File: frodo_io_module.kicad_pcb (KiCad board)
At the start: 4 copper layers, 60 x 60 mm, 162 parts, among them J1 Conn_02x04_Top_Bottom, J10 JST-GH 4Pin, J11 JST-GH 4Pin, J14 Conn_02x03_Odd_Even, J16 USB_C_Receptacle_USB2.0, J17 TC2050, J2 Conn_02x10_Odd_Even, J3 Conn_02x04_Top_Bottom, J4 Conn_02x03_Odd_Even, J6 JST-GH 4Pin, J7 JST-GH 4Pin, J8 JST-GH 4Pin, J9 JST-GH 4Pin, Q1 AOSP21321, Q2 AOSP21321, Q3 NMOS, Q4 NMOS, Q5 AOSP21321, Q6 AOSP21321, Q7 NMOS, Q8 NMOS, SW1 KMR721NGLFS, SW2 KMR721NGLFS, SW3 KMR721NGLFS, U1 L7805, U10 MCP2562-E-SN, U11 TPD4E1U06, U12 INA181A1, U2 L7805, U3 STM32F105RCTx, U5 AZ1117-3.3, U6 W25Q128JVP, U7 MCP2562-E-SN, U8 TPD4E1U06, U9 INA181A1, Y1 8MHz 12pF

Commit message: small routing improvements
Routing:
- net +3.3V: track 368.6 -> 370.0 mm
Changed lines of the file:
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@@
 	)
 	(segment
-		(start 145.734 104.156)
-		(end 145.734 107.932496)
-		(width 0.5)
-		(layer "F.Cu")
-		(net 2)
-	)
-	(segment
 		(start 110.78 117.05)
 		(end 110.29 117.54)
@@
 	)
 	(segment
+		(start 145.734 107.932496)
+		(end 145.734 104.156)
+		(width 0.5)
+		(layer "F.Cu")
+		(net 2)
+	)
+	(segment
 		(start 119.216182 124.334)
 		(end 122.484 124.334)
@@
 	)
 	(segment
-		(start 145.74 104.15)
-		(end 145.734 104.156)
-		(width 0.5)
-		(layer "F.Cu")
-		(net 2)
-	)
-	(segment
 		(start 111.02 117.29)
 		(end 110.78 117.05)
@@
 	)
 	(segment
+		(start 145.734 104.156)
+		(end 145.74 104.15)
+		(width 0.5)
+		(layer "F.Cu")
+		(net 2)
+	)
+	(segment
 		(start 121.230002 104.000002)
 		(end 120.25 104.000002)
@@
 	)
 	(via
-		(at 145.74 104.15)
-		(size 0.5)
-		(drill 0.25)
-		(layers "F.Cu" "B.Cu")
-		(net 2)
-	)
-	(via
 		(at 144.54 114.08)
 		(size 0.5)
@@
 	)
 	(via
+		(at 145.74 104.15)
+		(size 0.5)
+		(drill 0.3)
+		(layers "F.Cu" "B.Cu")
+		(net 2)
+	)
+	(via
 		(at 122.27 101.9)
 		(size 0.5)
@@
 	)
 	(segment
+		(start 145.74 105.0746)
+		(end 145.8722 105.2068)
+		(width 0.5)
+		(layer "B.Cu")
+		(net 2)
+	)
+	(segment
 		(start 122.752 101.9)
 		(end 122.27 101.9)
@@
 	)
 	(segment
+		(start 145.74 104.15)
+		(end 145.659 104.15)
+		(width 0.5)
+		(layer "B.Cu")
+		(net 2)
+	)
+	(segment
 		(start 107.242847 140.172847)
 		(end 108.752847 140.172847)
@@
 	)
 	(segment
+		(start 145.74 104.15)
+		(end 145.74 105.0746)
+		(width 0.5)
+		(layer "B.Cu")
+		(net 2)
+	)
+	(segment
 		(start 101.75 109.03)
 		(end 101.75 108.93)
@@
 	)
 	(segment
+		(start 145.659 104.15)
+		(end 144.6022 105.2068)
+		(width 0.5)
+		(layer "B.Cu")
+		(net 2)
+	)
+	(segment
 		(start 137.300001 133.75)
 		(end 135.6956 133.75)
@@
 	)
 	(segment
-		(start 145.25 105.2068)
-		(end 145.25 104.64)
-		(width 0.5)
-		(layer "B.Cu")
-		(net 2)
-	)
-	(segment
 		(start 134.886546 143.921)
 		(end 112.461 143.921)
@@
 	)
 	(segment
-		(start 145.25 104.64)
-		(end 145.74 104.15)
-		(width 0.5)
-		(layer "B.Cu")
-		(net 2)
-	)
-	(segment
 		(start 133.7706 123.7706)
 		(end 133.75 123.75)
@@
 	)
 	(segment
+		(start 144.06 100.77)
+		(end 147.3 104.01)
+		(width 0.5)
+		(layer "F.Cu")
+		(net 5)
+	)
+	(segment
 		(start 117.045 123)
 		(end 117.3 123.255)
@@
 	)
 	(segment
+		(start 136.22 101.19)
+		(end 136.64 100.77)
+		(width 0.5)
+		(layer "F.Cu")
+		(net 5)
+	)
+	(segment
+		(start 136.64 100.77)
+		(end 144.06 100.77)
+		(width 0.5)
+		(layer "F.Cu")
+		(net 5)
+	)
+	(segment
 		(start 107.09 141.45)
 		(end 107.33 141.21)
@@
 	)
 	(segment
-		(start 136.22 101.19)
-		(end 144.48 101.19)
-		(width 0.5)
-		(layer "F.Cu")
-		(net 5)
-	)
-	(segment
 		(start 116.84 116.67)
 		(end 114.75 116.67)
@@
 	)
 	(segment
-		(start 144.48 101.19)
-		(end 147.3 104.01)
-		(width 0.5)
-		(layer "F.Cu")
-		(net 5)
-	)
-	(segment
 		(start 106.2 109.380001)
 		(end 107.650001 107.93)
@@
 			(pts
 				(xy 110.53 136.78) (xy 110.53 137.92) (xy 110.62 138.01) (xy 110.62 138.22) (xy 110.35 138.49) (xy 110.41 139.76)
-				(xy 110.61 140.08) (xy 114.02 140.07) (xy 114.59 139.5) (xy 114.59 139.41) (xy 116.67 139.59) (xy 116.92 140.89)
-				(xy 117.71 142.06) (xy 117.71 142.96) (xy 119.53 144.64) (xy 120.1 145.22) (xy 121.26 145.26) (xy 122.18 144.2)
-				(xy 122.3 142.87) (xy 122.31 142.73) (xy 122.44 142.61) (xy 123.78 141.62) (xy 123.81 140.47) (xy 121.83 140.46)
-				(xy 121.82 140.47) (xy 121.83 140.86) (xy 121.69 141.08) (xy 120.04 141.1) (xy 118.75 140.06) (xy 118.75 138.74)
-				(xy 117.17 137.16) (xy 115.41 137.16) (xy 114.92 137.65) (xy 113.3 137.65) (xy 112.43 136.78) (xy 112.43 136.58)
-				(xy 112.11 136.26) (xy 111.05 136.26)
+				(xy 110.61 140.08) (xy 114.02 140.07) (xy 114.45 139.62) (xy 114.63 139.45) (xy 116.294247 139.442932)
+				(xy 116.81 139.85) (xy 116.82 140.98) (xy 117.55 141.81) (xy 117.55 142.83) (xy 119.43 144.73) (xy 119.9 145.21)
+				(xy 121.51 145.21) (xy 122.31 144.45) (xy 122.31 143.52) (xy 122.31 143.13) (xy 122.77 142.76) (xy 123.78 141.94)
+				(xy 123.81 140.47) (xy 121.83 140.46) (xy 121.82 140.47) (xy 121.83 140.86) (xy 121.69 141.08) (xy 120.04 141.1)
+				(xy 118.75 140.06) (xy 118.75 138.74) (xy 117.17 137.16) (xy 115.41 137.16) (xy 114.94 137.2) (xy 112.92 137.19)
+				(xy 112.43 136.78) (xy 112.43 136.58) (xy 112.11 136.26) (xy 111.05 136.26)
 			)
 		)
@@
 			(pts
 				(xy 127.47 146.1) (xy 127.14 146.43) (xy 127.14 148.26) (xy 127.83 148.5) (xy 132 148.56) (xy 132.83 147.89)
-				(xy 132.8 145.9) (xy 131.54 144.64) (xy 131.54 140.67) (xy 131.07 140.04) (xy 130.05 140.03) (xy 129.49 140.04)
-				(xy 129.09 140.43) (xy 129.06 145.26) (xy 128.58 145.83) (xy 127.8 145.82)
+				(xy 132.8 145.9) (xy 131.54 144.64) (xy 131.54 140.67) (xy 131.07 140.05) (xy 130.06 140.05) (xy 129.43 140.05)
+				(xy 129.07 140.42) (xy 129.06 145.26) (xy 128.58 145.83) (xy 127.8 145.82)
 			)
 		)
@@
 		(polygon
 			(pts
-				(xy 114.3 139.98) (xy 114.3 142.4) (xy 114.57 142.67) (xy 114.57 144.63) (xy 114.96 145.02) (xy 115.68 145.63)
-				(xy 115.83 145.85) (xy 115.92 146.02) (xy 115.92 148.55) (xy 116.36 148.99) (xy 119.98 148.97) (xy 120.64 148.34)
-				(xy 120.6 146.17) (xy 117.31 142.88) (xy 117.31 141.8) (xy 116.63 141.04) (xy 116.61 139.93) (xy 116.19 139.63)
-				(xy 114.84 139.62) (xy 114.37 139.91)
+				(xy 114.29 139.98) (xy 114.29 142.4) (xy 114.51 142.67) (xy 114.52 144.63) (xy 114.938515 145.009584)
+				(xy 115.6 145.65) (xy 115.78 145.87) (xy 115.91 146.12) (xy 115.91 148.55) (xy 116.35 148.99) (xy 119.97 148.97)
+				(xy 120.63 148.34) (xy 120.59 146.17) (xy 117.3 142.88) (xy 117.3 141.8) (xy 116.62 141.04) (xy 116.6 139.93)
+				(xy 116.18 139.63) (xy 114.65 139.62) (xy 114.36 139.91)
 			)
 		)
@@
 		(polygon
 			(pts
-				(xy 127.03 136.2) (xy 126.23 136.2) (xy 125.54 136.68) (xy 125.55 137.69) (xy 125.03 138.21) (xy 125 138.21)
-				(xy 124.99 140.66) (xy 125.52 141.15) (xy 127.82 141.13) (xy 129.34 139.59) (xy 130.97 139.59) (xy 132.05 140.67)
-				(xy 132.05 143.22) (xy 134.14 145.52) (xy 135.85 145.54) (xy 136.66 144.8) (xy 136.69 143.87) (xy 136.988329 143.445692)
-				(xy 138.157493 142.982177) (xy 138.3975 142.64) (xy 138.42 141.89) (xy 138.42 140.81) (xy 138.35 140.74)
-				(xy 136.83 140.74) (xy 136.25 141.32) (xy 134.31 141.32) (xy 134.05 140.95) (xy 133.37 138.3) (xy 130.23456 138.12494)
-				(xy 128.63 136.56)
+				(xy 127.77 136.2) (xy 126.23 136.2) (xy 125.54 136.68) (xy 125.55 137.69) (xy 125.03 138.21) (xy 125 138.24)
+				(xy 124.99 140.66) (xy 125.52 141.15) (xy 127.82 141.13) (xy 129.34 139.59) (xy 130.97 139.59) (xy 132.24 141.27)
+				(xy 132.24 144.41) (xy 133.27 145.53) (xy 135.85 145.53) (xy 136.66 144.8) (xy 136.69 143.87) (xy 136.988329 143.445692)
+				(xy 137.87 142.56) (xy 138.18 142.21) (xy 138.41 142.01) (xy 138.42 140.81) (xy 138.35 140.74) (xy 136.83 140.74)
+				(xy 136.25 141.32) (xy 134.31 141.32) (xy 134.05 140.95) (xy 133.54 138.962499) (xy 132.5 138.11)
+				(xy 130.23456 138.12494) (xy 128.39 136.2)
 			)
 		)
@@
 			(pts
 				(xy 124.35 142.8) (xy 123.2 143.95) (xy 123.21 145.16) (xy 122.03 146.28) (xy 122.04 148) (xy 122.8425 148.8025)
-				(xy 125.83 148.75) (xy 126.9 147.77) (xy 126.94 146.21) (xy 127.54 145.55) (xy 128.45 145.61) (xy 128.96 145.03)
+				(xy 125.74 148.8) (xy 126.94 147.78) (xy 126.94 146.21) (xy 127.54 145.61) (xy 128.45 145.61) (xy 128.96 145.03)
 				(xy 128.97 143.31) (xy 128.41 142.8)
 			)

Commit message: improve silkscreen
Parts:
- moved R32 0.60 mm to (118.5, 105.1)
- moved R3 0.54 mm to (101.8, 127.6)
- moved U2 0.54 mm to (107.0, 125.7)
- moved D12 0.44 mm to (118.5, 102.6)
- moved D10 0.30 mm to (116.8, 102.6)
- moved R30 0.29 mm to (116.8, 105.1)
- moved D9 0.17 mm to (115.0, 102.6)
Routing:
- net USB_D-: track 12.5 -> 13.2 mm
- net Net-(D4-A): track 20.6 -> 21.2 mm
- net STAT_LED2: track 31.2 -> 30.7 mm
- net USB_D+: track 12.2 -> 12.8 mm
- net GND: vias 69 -> 105
- added copper zone on F.Cu, net main_voltage
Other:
- board text added: "3"
- board text added: "3,3V"
- board text added: "3,3V/5V"
- board text added: "5V"
- board text removed: "o1|vcc"
- board text removed: "o2|sig"
- board text removed: "o3|sig"
- board text removed: "o3|vcc"

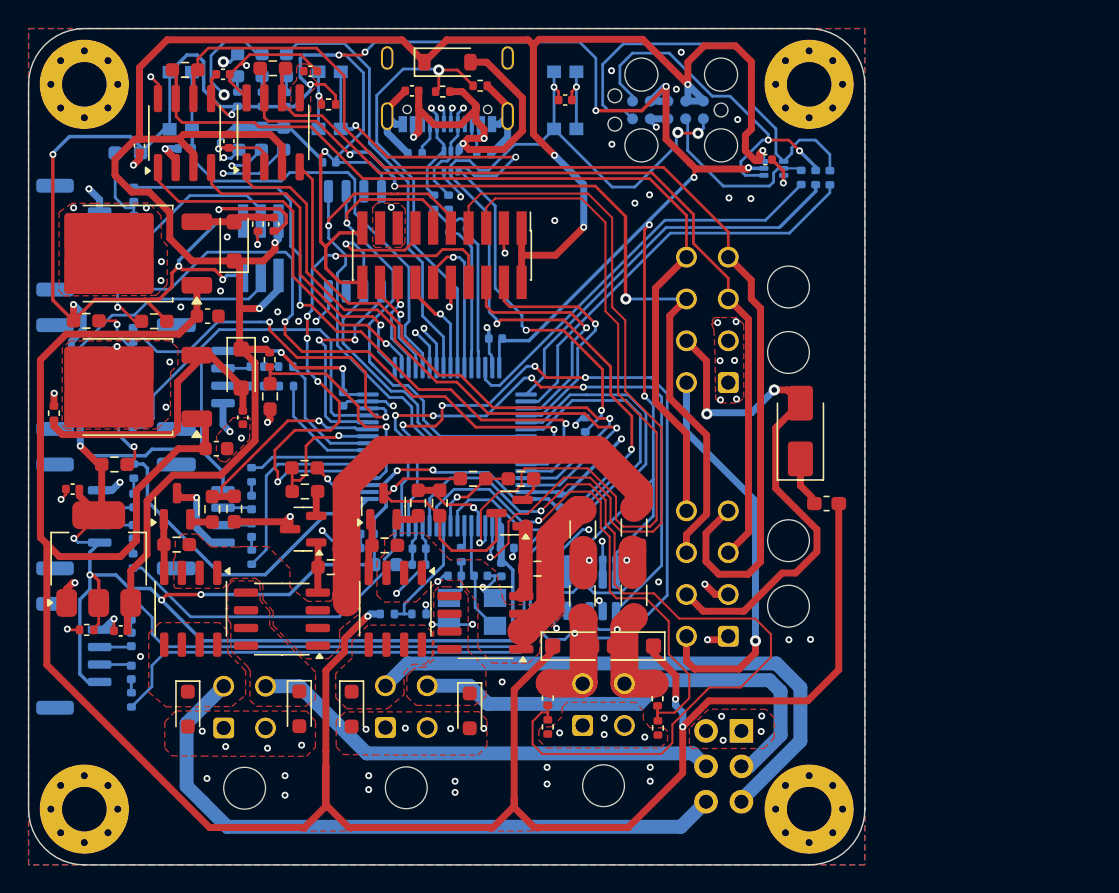
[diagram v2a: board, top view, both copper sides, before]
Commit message: Fix ouput silkscreen number, clearance violation, start skew tuning (CAN)
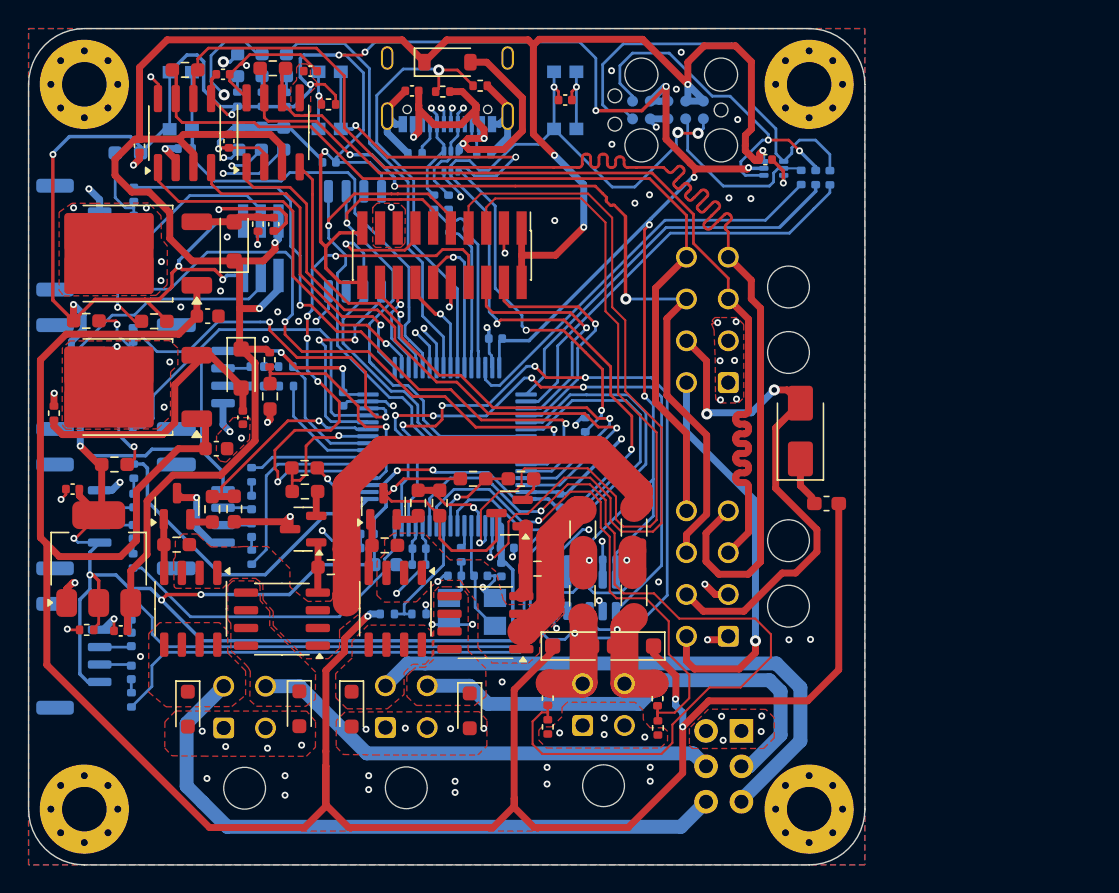
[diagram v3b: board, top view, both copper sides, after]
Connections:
- net CAN_1_H renamed CAN_1+
- net CAN_1_L renamed CAN_1-
- net CAN_2_H renamed CAN_2+
- net CAN_2_L renamed CAN_2-
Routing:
- net CAN_2-: track 82.8 -> 97.3 mm
- net CAN_1-: track 63.0 -> 68.2 mm

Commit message: improve silkscreen
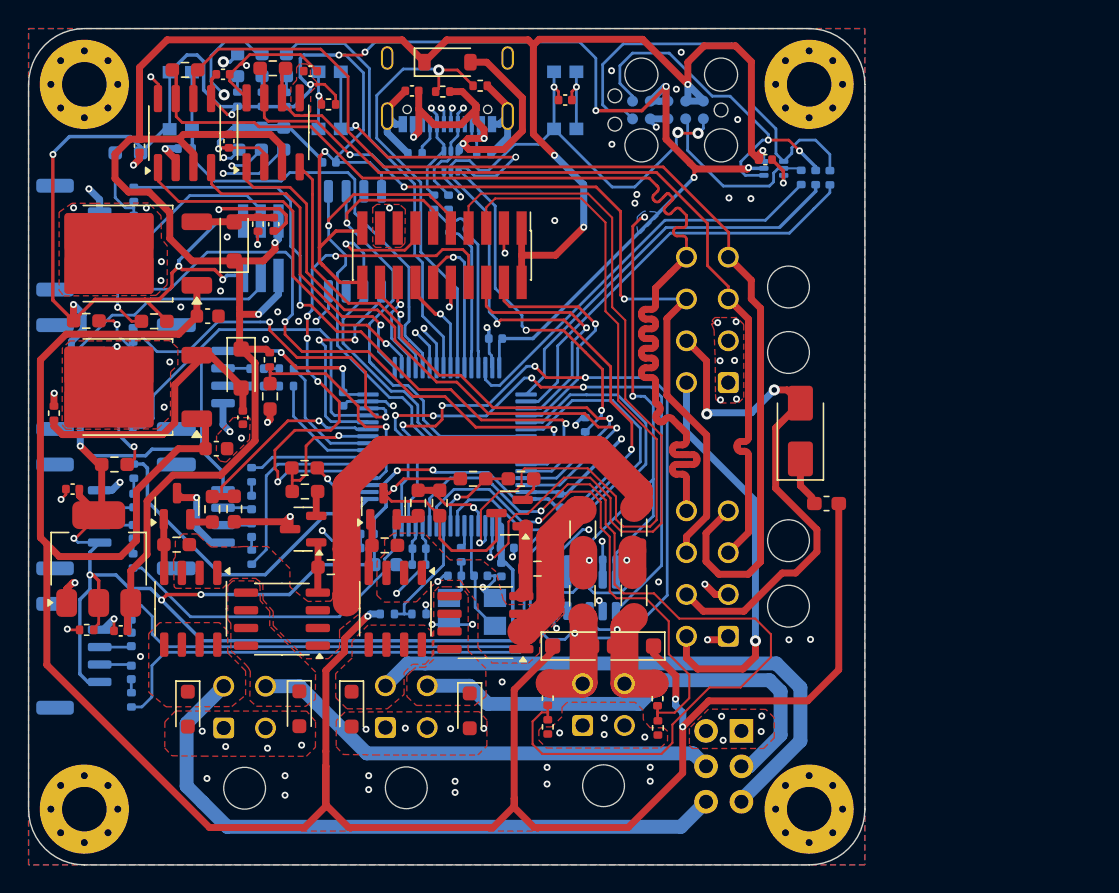
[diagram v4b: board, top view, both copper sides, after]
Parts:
- moved R20 0.16 mm to (118.5, 124.4)
- moved FB10 0.15 mm to (116.4, 124.4)
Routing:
- net CAN_2+: track 65.7 -> 81.7 mm
- net CAN_2-: track 97.3 -> 82.5 mm
- net CAN_1-: track 68.2 -> 64.4 mm
- net +3.3V: track 370.4 -> 372.6 mm
- net CAN_1+: track 64.2 -> 63.6 mm
- net COM4_2: track 60.6 -> 60.0 mm
- added copper zone on B.Cu, net +3.3V
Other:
- board text added: "+"
- board text added: "O1|O2 gnd|gnd"
- board text added: "O3|O4 gnd|gnd"
- board text added: "V1|V2 gnd|gnd"
- board text removed: "3,3V/5V"
- board text removed: "o1|o2 gnd|gnd"
- board text removed: "o3|o4 gnd|gnd"
- board text removed: "v2|v1 gnd|gnd"

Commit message: Revisit can trace tuning
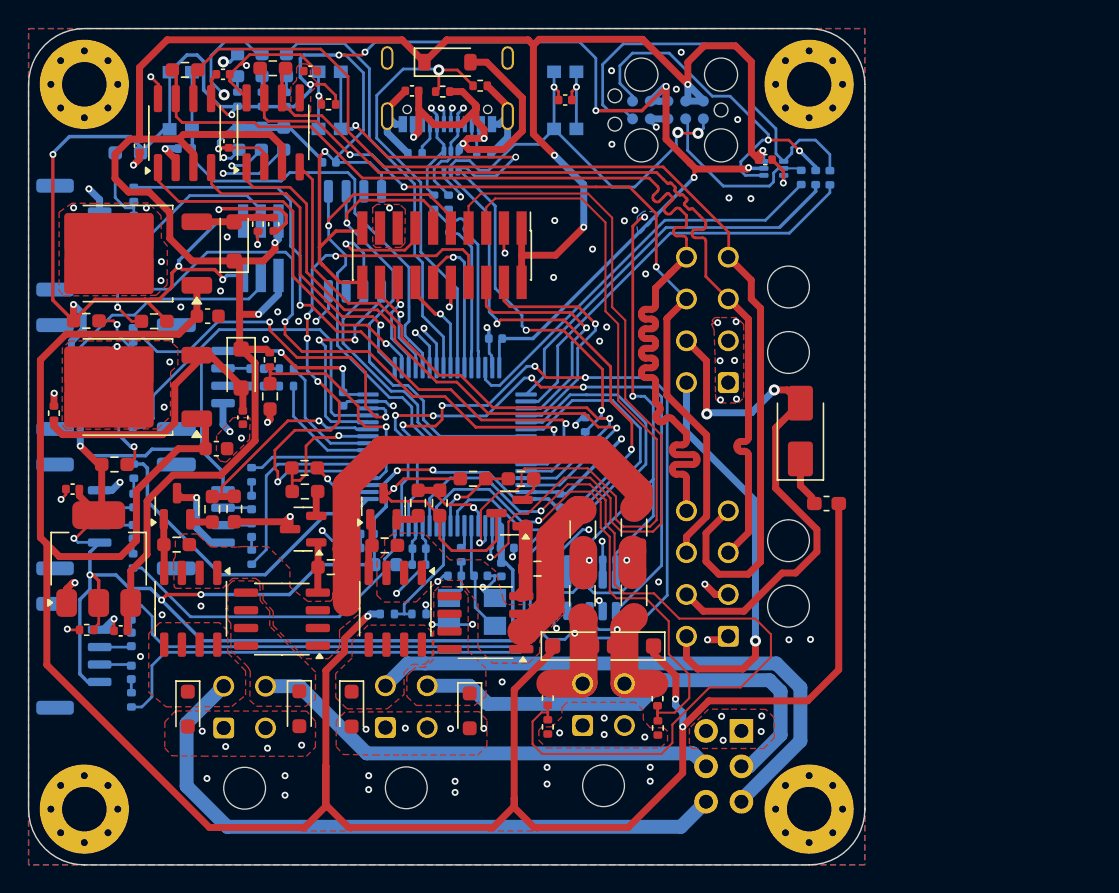
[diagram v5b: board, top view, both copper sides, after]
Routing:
- net GND: track 168.5 -> 161.1 mm, vias 105 -> 112
- net +3.3V: track 372.6 -> 370.0 mm
- net IO-3 (ADC): track 8.71 -> 6.54 mm
- net CAN_1+: track 63.6 -> 61.8 mm
- net IO-5: track 8.19 -> 6.44 mm
- net SPI1_MISO: track 31.9 -> 30.5 mm
- net SPI1_MOSI: track 40.7 -> 39.8 mm
- net VS2: track 20.6 -> 19.8 mm
- net VS1: track 19.5 -> 18.7 mm
- net IO-8: track 11.2 -> 10.4 mm
- net CAN_2-: track 82.5 -> 81.8 mm
- net SPI_CS_FLASH: track 15.7 -> 15.0 mm
- net +5V: track 168.1 -> 167.5 mm
- net SH22: track 7.98 -> 7.40 mm
- net /D0-: track 11.1 -> 10.6 mm
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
